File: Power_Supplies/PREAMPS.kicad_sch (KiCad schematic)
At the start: 35 parts, among them J3 XLR3, J5 AudioJack3, SW1 SW_Push, U12 SSM2019BRNZ, U13 OPA2134

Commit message: Add files via upload
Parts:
- removed C102, C32: 470pf, symbol Device:C_Polarized_US
- removed C107: 47uF, Capacitor_SMD:CP_Elec_4x5.8, symbol Device:C_Polarized_US
- removed D1: LED, LED_THT:LED_D5.0mm, symbol PCM_SL_Devices:LED
- removed J3: XLR3, symbol Connector_Audio:XLR3
- removed J5: AudioJack3, symbol Connector_Audio:AudioJack3
- removed R30, R31: 5.1k, Resistor_SMD:R_0805_2012Metric, symbol Device:R
- removed R32: 47, Resistor_SMD:R_0805_2012Metric, symbol Device:R
- removed SW1: SW_Push, Button_Switch_THT:SW_PUSH_1P1T_6x3.5mm_H5.0_APEM_MJTP1250, symbol Switch:SW_Push
- added C116: 10uF, Capacitor_SMD:CP_Elec_4x5.8, symbol Device:C_Polarized_US
- added C117, C120: 200pF, Capacitor_SMD:C_0402_1005Metric, symbol Device:C
- added D2: LED, LED_SMD:LED_0201_0603Metric, symbol PCM_SL_Devices:LED
- added J6: XLR3_AudioJack2_Combo, SamacSys_Parts:FA-238_EPS, symbol Connector_Audio:XLR3_AudioJack2_Combo
- added R46: 2.2k, Resistor_SMD:R_0805_2012Metric, symbol Device:R
- added R47, R56: 5.1k, Resistor_SMD:R_0805_2012Metric, symbol Device:R
- added SW2: SW_Push, Button_Switch_THT:SW_PUSH_1P1T_6x3.5mm_H5.0_APEM_MJTP1250, symbol Switch:SW_Push
- RV1, RV2: footprint (none) -> Potentiometer_THT:Potentiometer_ACP_CA9-V10_Vertical
- U12: footprint R_8_ADI -> SamacSys_Parts:SOIC127P600X175-8N
- U13: footprint (none) -> Package_SO:SOIC-8_3.9x4.9mm_P1.27mm
- renumbered DZ2 to DZ10, DZ4 to DZ11, DZ3 to DZ12, DZ1 to DZ9, R33 to R60
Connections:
- net 36V: now also SW2.2
- net AGND: now also C116.2, C117.1, C120.1, J6.1, J6.S, R46.2
- net at C110.1: now also C117.2, J6.2, R47.2
- net at C111.1: now also C120.2, J6.3, R56.2
- net at C115.2: now also J6.T
- new net: D2.1, R46.1
- new net: C116.1, D2.2, R47.1, R56.1, SW2.1
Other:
- moved on the sheet: C110, C111, C112, C113, C114, C115, C118, C119, DZ10, DZ11, DZ12, DZ9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

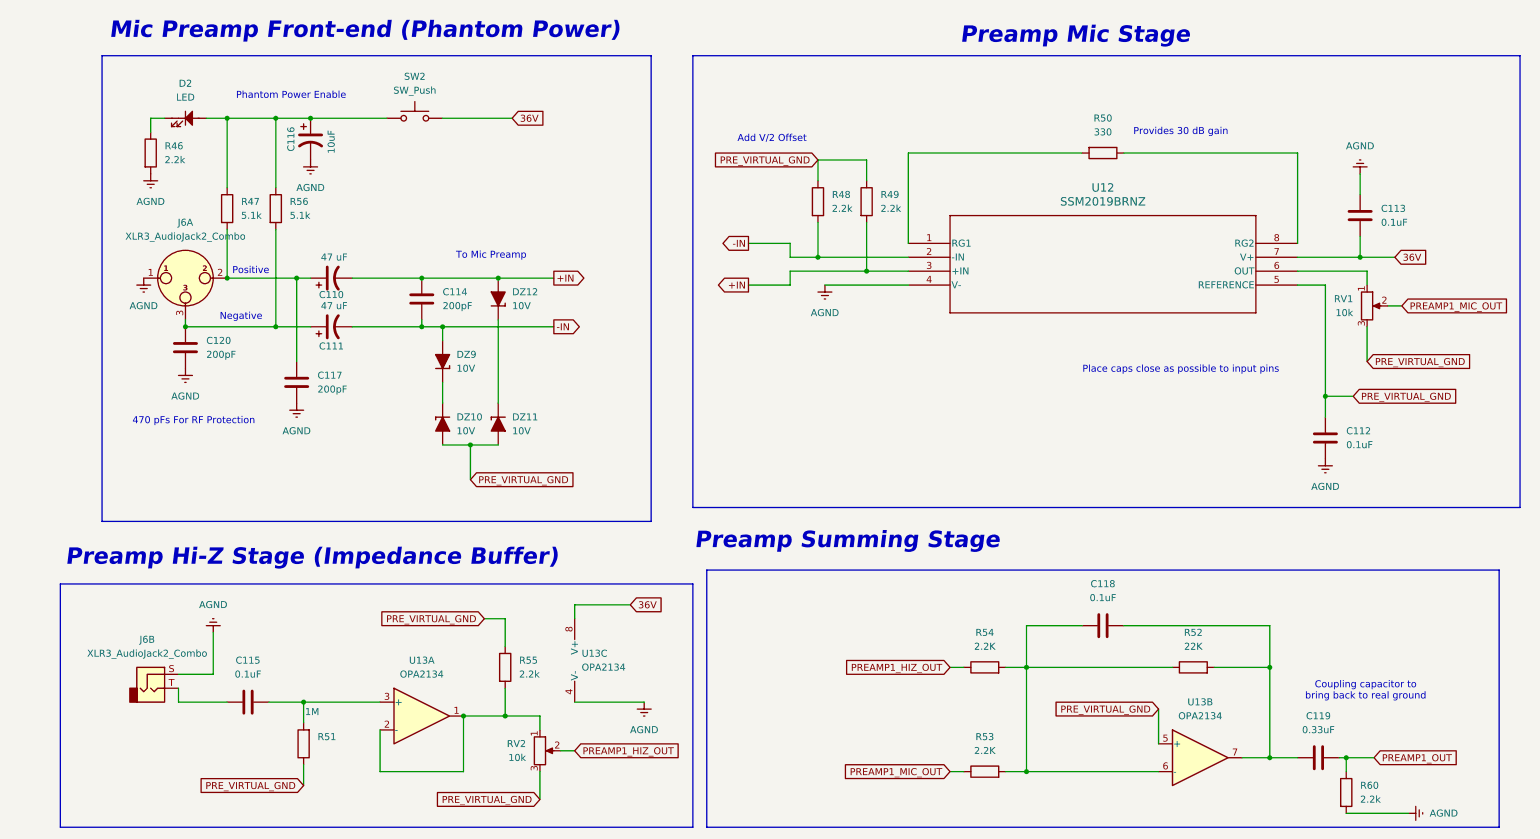
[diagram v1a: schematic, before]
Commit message: New preamp design + some added files
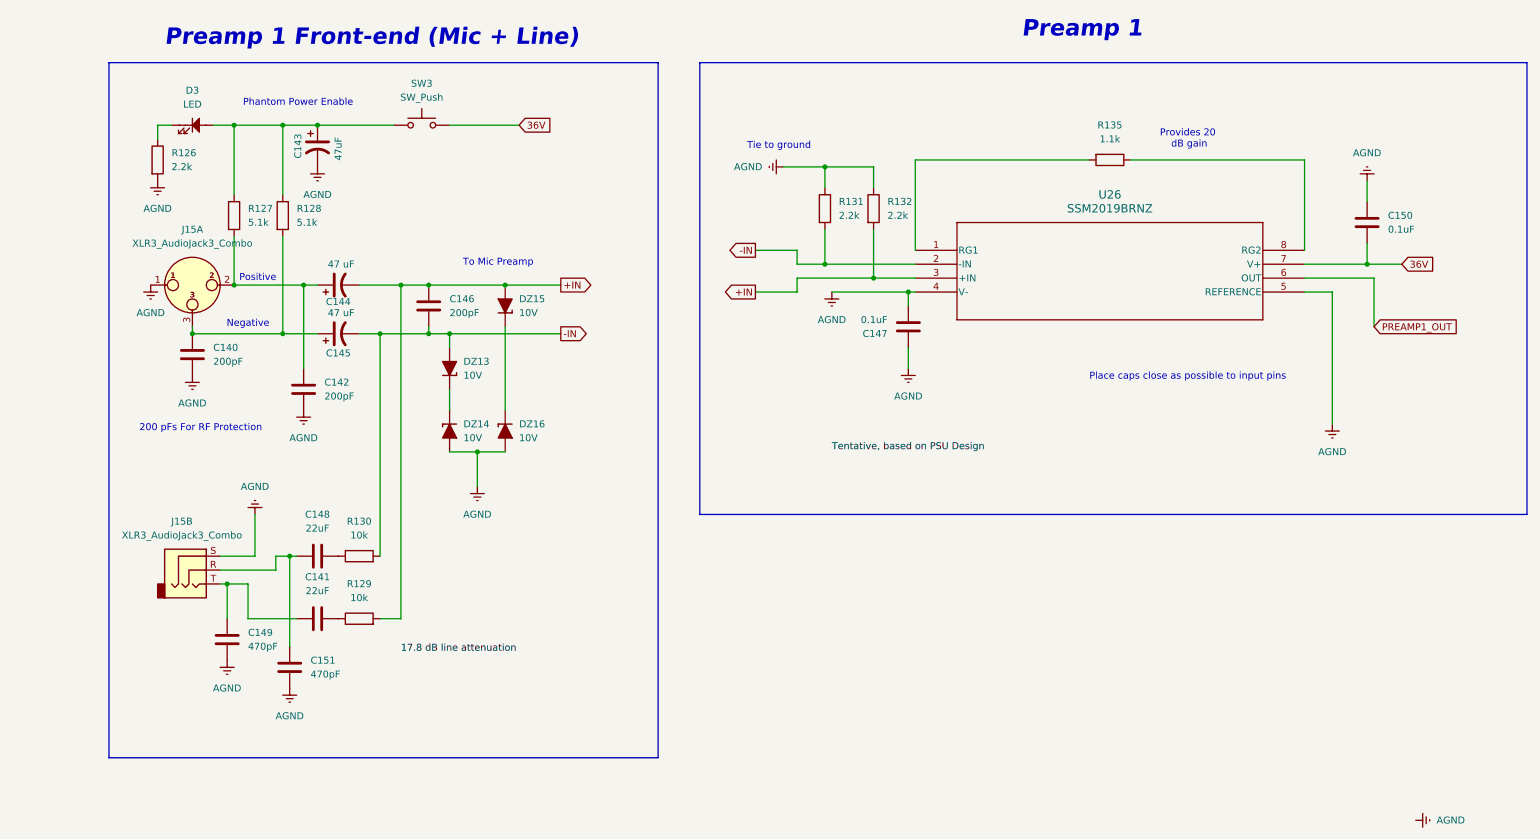
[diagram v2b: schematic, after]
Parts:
- removed C110, C111: 47 uF, Capacitor_SMD:CP_Elec_4x5.8, symbol Device:C_Polarized_US
- removed C112, C113, C115, C118: 0.1uF, Capacitor_SMD:C_0402_1005Metric, symbol Device:C
- removed C114, C117, C120: 200pF, Capacitor_SMD:C_0402_1005Metric, symbol Device:C
- removed C116: 10uF, Capacitor_SMD:CP_Elec_4x5.8, symbol Device:C_Polarized_US
- removed C119: 0.33uF, Capacitor_SMD:C_0402_1005Metric, symbol Device:C
- removed D2: LED, LED_SMD:LED_0201_0603Metric, symbol PCM_SL_Devices:LED
- removed DZ10, DZ11, DZ12, DZ9: 10V, Diode_SMD:D_SMB, symbol PCM_Diode_Zener_AKL:D_Zener_Generic
- removed J6: XLR3_AudioJack2_Combo, SamacSys_Parts:FA-238_EPS, symbol Connector_Audio:XLR3_AudioJack2_Combo
- removed R46, R48, R49, R55, R60: 2.2k, Resistor_SMD:R_0805_2012Metric, symbol Device:R
- removed R47, R56: 5.1k, Resistor_SMD:R_0805_2012Metric, symbol Device:R
- removed R50: 330, Resistor_SMD:R_0805_2012Metric, symbol Device:R
- removed R51: 1M, Resistor_SMD:R_0805_2012Metric, symbol Device:R
- removed R52: 22K, Resistor_SMD:R_0805_2012Metric, symbol Device:R
- removed R53, R54: 2.2K, Resistor_SMD:R_0805_2012Metric, symbol Device:R
- removed RV1, RV2: 10k, Potentiometer_THT:Potentiometer_ACP_CA9-V10_Vertical, symbol Device:R_Potentiometer
- removed SW2: SW_Push, Button_Switch_THT:SW_PUSH_1P1T_6x3.5mm_H5.0_APEM_MJTP1250, symbol Switch:SW_Push
- removed U12: SSM2019BRNZ, SamacSys_Parts:SOIC127P600X175-8N, symbol SDLibrary:SSM2019BRNZ
- removed U13: OPA2134, Package_SO:SOIC-8_3.9x4.9mm_P1.27mm, symbol Amplifier_Operational:OPA2134
- added C140, C142, C146: 200pF, Capacitor_SMD:C_0402_1005Metric, symbol Device:C
- added C141, C148: 22uF, Capacitor_SMD:C_0402_1005Metric, symbol Device:C
- added C143: 47uF, Capacitor_SMD:CP_Elec_4x5.8, symbol Device:C_Polarized_US
- added C144, C145: 47 uF, Capacitor_SMD:CP_Elec_4x5.8, symbol Device:C_Polarized_US
- added C147, C150: 0.1uF, Capacitor_SMD:C_0402_1005Metric, symbol Device:C
- added C149, C151: 470pF, Capacitor_SMD:C_0402_1005Metric, symbol Device:C
- added D3: LED, LED_SMD:LED_0201_0603Metric, symbol PCM_SL_Devices:LED
- added DZ13, DZ14, DZ15, DZ16: 10V, Diode_SMD:D_SMB, symbol PCM_Diode_Zener_AKL:D_Zener_Generic
- added J15: XLR3_AudioJack3_Combo, symbol Connector_Audio:XLR3_AudioJack3_Combo
- added R126, R131, R132: 2.2k, Resistor_SMD:R_0805_2012Metric, symbol Device:R
- added R127, R128: 5.1k, Resistor_SMD:R_0805_2012Metric, symbol Device:R
- added R129, R130: 10k, Resistor_SMD:R_0805_2012Metric, symbol Device:R
- added R135: 1.1k, Resistor_SMD:R_0805_2012Metric, symbol Device:R
- added SW3: SW_Push, Button_Switch_THT:SW_PUSH_1P1T_6x3.5mm_H5.0_APEM_MJTP1250, symbol Switch:SW_Push
- added U26: SSM2019BRNZ, SamacSys_Parts:SOIC127P600X175-8N, symbol SDLibrary:SSM2019BRNZ
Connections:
- net +IN: now also C144.2, C146.2, DZ15.2 (A), R129.2, R132.2, U26.3 (+IN)
- net -IN: now also C145.2, C146.1, DZ13.2 (A), R130.2, R131.2, U26.2 (-IN)
- net 36V: now also C150.1, SW3.2, U26.7 (V+)
- net AGND: now also C140.1, C142.1, C143.2, C147.1, C147.2, C149.1, C150.2, C151.1, DZ14.2 (A), DZ16.2 (A), J15.1, J15.S, R126.2, R131.1, R132.1, U26.4 (V-), U26.5 (REFERENCE)
- net PREAMP1_OUT: now also U26.6 (OUT)
- new net: C140.2, C145.1, J15.3, R128.2
- new net: R135.1, U26.8 (RG2)
- new net: R135.2, U26.1 (RG1)
- new net: C143.1, D3.2, R127.1, R128.1, SW3.1
- new net: C148.2, C151.2, J15.R
- new net: C141.2, C149.2, J15.T
- new net: C141.1, R129.1
- new net: D3.1, R126.1
- new net: DZ15.1 (K), DZ16.1 (K)
- new net: DZ13.1 (K), DZ14.1 (K)
- new net: C148.1, R130.1
- new net: C142.2, C144.1, J15.2, R127.2
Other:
- note added: "200 pFs For RF Protection"
- note added: "Preamp 1"
- note added: "Preamp 1 Front-end (Mic + Line)"
- note added: "Provides 20 dB gain"
- note added: "Tie to ground"
- note removed: "470 pFs For RF Protection"
- note removed: "Add V/2 Offset"
- note removed: "Coupling capacitor to bring back to real ground"
- note removed: "Mic Preamp Front-end (Phantom Power)"
- note removed: "Preamp Hi-Z Stage (Impedance Buffer)"
- note removed: "Preamp Mic Stage"
- note removed: "Preamp Summing Stage"
- note removed: "Provides 30 dB gain"

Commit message: Finished HiZ Inputs
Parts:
- added C152, C154, C156, C157: 0.01uF, Capacitor_SMD:C_0402_1005Metric, symbol Device:C
- added C153, C155, C158, C159: 0.1uF, Capacitor_SMD:C_0402_1005Metric, symbol Device:C
- added J14, J16, J17, J18: AudioJack2, symbol Connector_Audio:AudioJack2
- added R133, R137, R140, R141: 1M, Resistor_SMD:R_0805_2012Metric, symbol Device:R
- added R134, R139, R144, R145: 2.2k, Resistor_SMD:R_0805_2012Metric, symbol Device:R
- added R136, R138, R142, R143: 1k, Resistor_SMD:R_0805_2012Metric, symbol Device:R
- added U25, U27: NE5532, symbol Amplifier_Operational:NE5532
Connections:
- net AGND: now also C153.1, C155.1, C158.1, C159.1, J14.S, J16.S, J17.S, J18.S, R133.1, R136.2, R137.1, R138.2, R140.1, R141.1, R142.2, R143.2
- new net: C157.2, J18.T
- new net: R144.1, U27.1
- new net: R142.1, R144.2, U27.2 (-)
- new net: C157.1, R141.2, U27.3 (+)
- new net: R134.1, U25.1
- new net: R134.2, R136.1, U25.2 (-)
- new net: C152.1, R133.2, U25.3 (+)
- new net: R139.1, U25.7
- new net: R138.1, R139.2, U25.6 (-)
- new net: C154.1, R137.2, U25.5 (+)
- new net: C156.1, R140.2, U27.5 (+)
- new net: R143.1, R145.2, U27.6 (-)
- new net: R145.1, U27.7
- new net: C156.2, J17.T
- new net: C154.2, J16.T
- new net: C152.2, J14.T
- new net -5V_1: C155.2, C159.2, U25.4 (V-), U27.4 (V-)
- new net 5V: C153.2, C158.2, U25.8 (V+), U27.8 (V+)
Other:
- note added: "Hi-Z Instrument Input 1 & 2"
- note added: "Hi-Z Instrument Input 3 & 4"

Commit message: Updated circuits, added some schematic pictures
Mostly just pushing so I can work on a different computer lol
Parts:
- removed U25, U27: NE5532, symbol Amplifier_Operational:NE5532
- added C160, C163, C169, C172, C175, C181, C184, C187, C193: 200pF, Capacitor_SMD:C_0402_1005Metric, symbol Device:C
- added C161, C162, C173, C174, C185, C186: 470pF, Capacitor_SMD:C_0402_1005Metric, symbol Device:C
- added C164, C176, C188: 47uF, Capacitor_SMD:CP_Elec_4x5.8, symbol Device:C_Polarized_US
- added C165, C166, C177, C178, C189, C190: 22uF, Capacitor_SMD:C_0402_1005Metric, symbol Device:C
- added C167, C168, C179, C180, C191, C192: 47 uF, Capacitor_SMD:CP_Elec_4x5.8, symbol Device:C_Polarized_US
- added C170, C171, C182, C183, C194, C195: 0.1uF, Capacitor_SMD:C_0402_1005Metric, symbol Device:C
- added D4, D5, D6: LED, LED_SMD:LED_0201_0603Metric, symbol PCM_SL_Devices:LED
- added DZ17, DZ18, DZ19, DZ20, DZ21, DZ22, DZ23, DZ24, DZ25, DZ26, DZ27, DZ28: 10V, Diode_SMD:D_SMB, symbol PCM_Diode_Zener_AKL:D_Zener_Generic
- added J19, J20, J21: XLR3_AudioJack3_Combo, symbol Connector_Audio:XLR3_AudioJack3_Combo
- added R146, R151, R152, R154, R159, R160, R162, R167, R168: 2.2k, Resistor_SMD:R_0805_2012Metric, symbol Device:R
- added R147, R148, R155, R156, R163, R164: 5.1k, Resistor_SMD:R_0805_2012Metric, symbol Device:R
- added R149, R150, R157, R158, R165, R166: 10k, Resistor_SMD:R_0805_2012Metric, symbol Device:R
- added R153, R161, R169: 1.1k, Resistor_SMD:R_0805_2012Metric, symbol Device:R
- added R170, R171, R172, R173: 47, Resistor_SMD:R_0805_2012Metric, symbol Device:R
- added SW7, SW8, SW9: SW_Push, Button_Switch_THT:SW_PUSH_1P1T_6x3.5mm_H5.0_APEM_MJTP1250, symbol Switch:SW_Push
- added U25, U27: OPA2134, symbol Amplifier_Operational:OPA2134
- added U28, U29, U30: SSM2019BRNZ, SamacSys_Parts:SOIC127P600X175-8N, symbol SDLibrary:SSM2019BRNZ
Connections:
- net -5V_1: now also C147.1, U26.4 (V-), C170.1, C182.1, C194.1, U25.4 (V-), U27.4 (V-), U28.4 (V-), U29.4 (V-), U30.4 (V-)
- net 36V: now also SW7.2, SW8.2, SW9.2; no longer C150.1, U26.7 (V+)
- net 5V: now also C150.1, U26.7 (V+), C171.1, C183.1, C195.1, U25.8 (V+), U27.8 (V+), U28.7 (V+), U29.7 (V+), U30.7 (V+)
- net AGND: now also C160.1, C161.1, C162.1, C163.1, C164.2, C170.2, C171.2, C172.1, C173.1, C174.1, C175.1, C176.2, C182.2, C183.2, C184.1, C185.1, C186.1, C187.1, C188.2, C194.2, C195.2, DZ18.2 (A), DZ20.2 (A), DZ22.2 (A), DZ24.2 (A), DZ26.2 (A), DZ28.2 (A), J19.1, J19.S, J20.1, J20.S, J21.1, J21.S, R146.2, R151.1, R152.1, R154.2, R159.1, R160.1, R162.2, R167.1, R168.1, U28.5 (REFERENCE), U29.5 (REFERENCE), U30.5 (REFERENCE); no longer C147.1, U26.4 (V-)
- net at C143.1, D3.2, R127.1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: now also R170.1; no longer SW3.1
- net INST3_OUT: now reaches R144.1
- net INST3_OUT: now also U27.1
- net at R142.1, R144.2: now also U27.2 (-)
- net at C157.1, R141.2: now also U27.3 (+)
- net INST1_OUT: now reaches R134.1
- net INST1_OUT: now also U25.1
- net at R134.2, R136.1: now also U25.2 (-)
- net at C152.1, R133.2: now also U25.3 (+)
- net INST2_OUT: now reaches R139.1
- net INST2_OUT: now also U25.7
- net at R138.1, R139.2: now also U25.6 (-)
- net at C154.1, R137.2: now also U25.5 (+)
- net at C156.1, R140.2: now also U27.5 (+)
- net at R143.1, R145.2: now also U27.6 (-)
- net INST4_OUT: now reaches R145.1
- net INST4_OUT: now also U27.7
- net +IN renamed +IN1
- net -IN renamed -IN1
- new net: C172.2, C180.1, J20.3, R156.2
- new net: D6.1, R162.1
- new net: C188.1, D6.2, R163.1, R164.1, R173.1
- new net: R170.2, SW3.1
- new net: C166.1, R150.1
- new net: C161.2, C166.2, J19.T
- new net: C175.2, C179.1, J20.2, R155.2
- new net: C177.1, R157.1
- new net: C174.2, C177.2, J20.R
- new net: R173.2, SW9.1
- new net: C184.2, C192.1, J21.3, R164.2
- new net: R172.2, SW8.1
- new net: C163.2, C167.1, J19.2, R147.2
- new net: DZ25.1 (K), DZ26.1 (K)
- new net: C173.2, C178.2, J20.T
- new net: R153.1, U28.8 (RG2)
- new net: R153.2, U28.1 (RG1)
- new net: C176.1, D5.2, R155.1, R156.1, R172.1
- new net: C189.1, R165.1
- new net: D4.1, R146.1
- new net: R171.2, SW7.1
- new net: C186.2, C189.2, J21.R
- new net: R161.1, U29.8 (RG2)
- new net: R161.2, U29.1 (RG1)
- new net: DZ27.1 (K), DZ28.1 (K)
- new net: DZ23.1 (K), DZ24.1 (K)
- new net: C162.2, C165.2, J19.R
- new net: C190.1, R166.1
- new net: C164.1, D4.2, R147.1, R148.1, R171.1
- new net: D5.1, R154.1
- new net: C187.2, C191.1, J21.2, R163.2
- new net: DZ17.1 (K), DZ18.1 (K)
- new net: C185.2, C190.2, J21.T
- new net: R169.2, U30.1 (RG1)
- new net: R169.1, U30.8 (RG2)
- new net: C165.1, R149.1
- new net: DZ21.1 (K), DZ22.1 (K)
- new net: DZ19.1 (K), DZ20.1 (K)
- new net: C160.2, C168.1, J19.3, R148.2
- new net: C178.1, R158.1
- new net +IN2: C167.2, C169.2, DZ19.2 (A), R150.2, R152.2, U28.3 (+IN)
- new net +IN3: C179.2, C181.2, DZ23.2 (A), R158.2, R160.2, U29.3 (+IN)
- new net +IN4: C191.2, C193.2, DZ27.2 (A), R166.2, R168.2, U30.3 (+IN)
- new net -IN2: C168.2, C169.1, DZ17.2 (A), R149.2, R151.2, U28.2 (-IN)
- new net -IN3: C180.2, C181.1, DZ21.2 (A), R157.2, R159.2, U29.2 (-IN)
- new net -IN4: C192.2, C193.1, DZ25.2 (A), R165.2, R167.2, U30.2 (-IN)
- new net PREAMP2_OUT: U28.6 (OUT)
- new net PREAMP3_OUT: U29.6 (OUT)
- new net PREAMP4_OUT: U30.6 (OUT)
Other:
- note added: "17.8 dB line attenuation Voltage divider R129 and R130 against R127||R132 and R128||131 respectively"
- note added: "Approx. 10 dB Gain G = 1 + (Rf/Rg)"
- note added: "Phantom Power"
- note added: "Place bypass caps as close to supply pins as possible"
- note added: "Preamp 1 (Mic + Line)"
- note added: "Preamp 2 (Mic + Line)"
- note added: "Preamp 3 (Mic + Line)"
- note added: "Preamp 4 (Mic + Line)"
- note removed: "Preamp 1"
- note removed: "Preamp 1 Front-end (Mic + Line)"
- moved on the sheet: C147, C150, R131, R132, R135, SW3, U26
